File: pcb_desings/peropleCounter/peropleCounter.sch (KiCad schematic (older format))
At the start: 7 parts

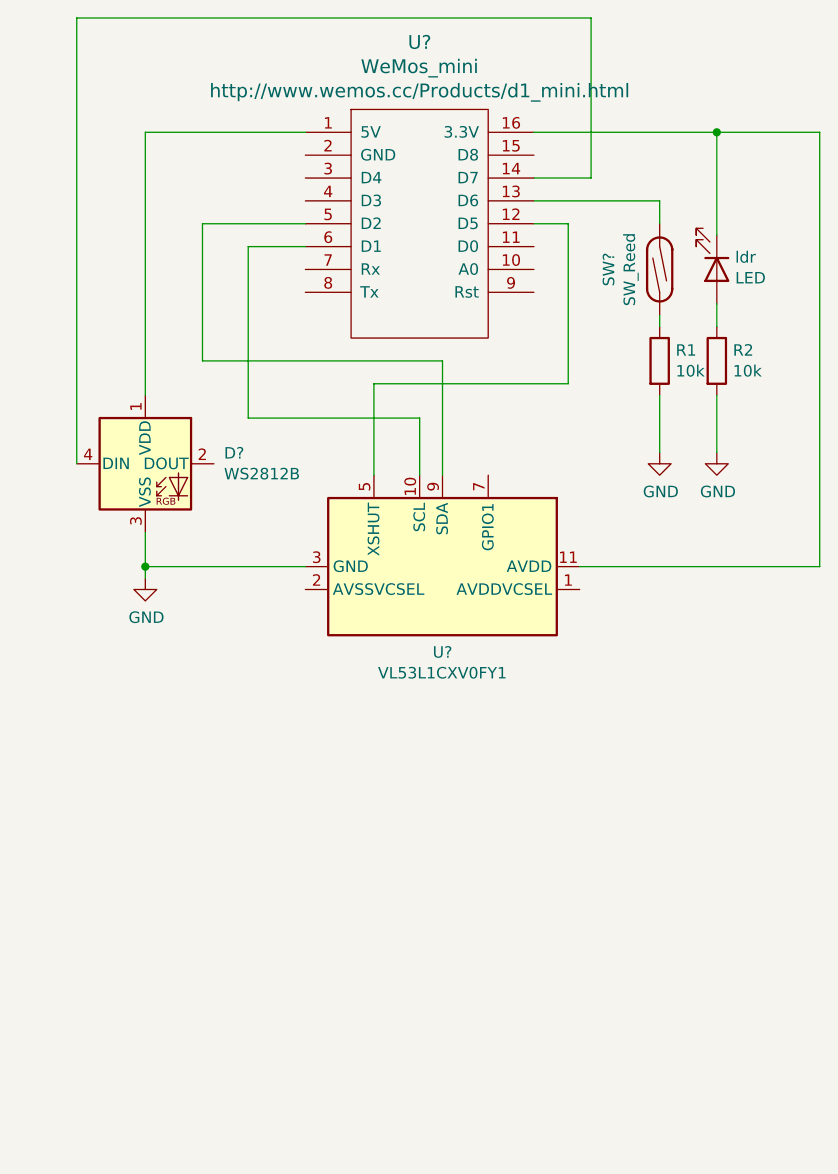
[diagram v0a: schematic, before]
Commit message: Fixed reed switch connection diagram and pin input
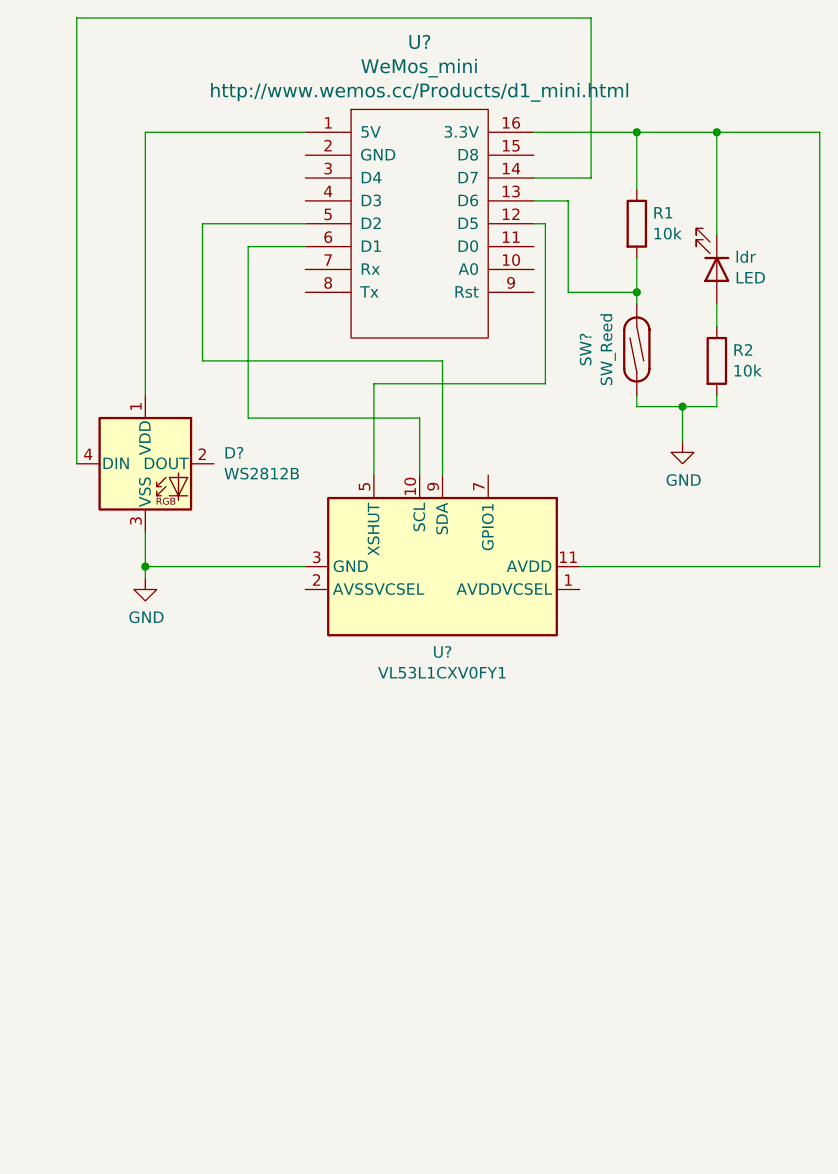
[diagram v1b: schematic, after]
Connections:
- net GND: now also SW?.1; no longer R1.2
- net at SW?.2, U?.13 (D6): now also R1.2
- net at U?.11 (AVDD), U?.16 (3.3V), ldr.1 (K): now also R1.1
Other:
- moved on the sheet: R1, SW?
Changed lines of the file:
@@
-$EndComp
-$Comp
-L Device:R R1
-U 1 1 60685B83
-P 3500 2250
-F 0 "R1" H 3570 2296 50  0000 L CNN
-F 1 "10k" H 3570 2205 50  0000 L CNN
-F 2 "" V 3430 2250 50  0001 C CNN
-F 3 "~" H 3500 2250 50  0001 C CNN
-	1    3500 2250
-	1    0    0    -1
-$EndComp
-$Comp
-L Switch:SW_Reed SW?
-U 1 1 60687B72
-P 3500 1850
-F 0 "SW?" H 3500 2072 50  0000 C CNN
-F 1 "SW_Reed" H 3500 1981 50  0000 C CNN
-F 2 "" H 3500 1850 50  0001 C CNN
-F 3 "~" H 3500 1850 50  0001 C CNN
-	1    3500 1850
-	0    -1   -1   0
 $EndComp
 $Comp
@@
 Wire Wire Line
 	3750 2100 3750 2000
-$Comp
-L power:GND #PWR?
-U 1 1 6068DD9C
-P 3750 2650
-F 0 "#PWR?" H 3750 2400 50  0001 C CNN
-F 1 "GND" H 3755 2477 50  0000 C CNN
-F 2 "" H 3750 2650 50  0001 C CNN
-F 3 "" H 3750 2650 50  0001 C CNN
-	1    3750 2650
-	1    0    0    -1
-$EndComp
-Wire Wire Line
-	3750 2650 3750 2400
-Wire Wire Line
-	2950 1250 3750 1250
-Wire Wire Line
-	3500 2100 3500 2050
-$Comp
-L power:GND #PWR?
-U 1 1 6068FDBC
-P 3500 2650
-F 0 "#PWR?" H 3500 2400 50  0001 C CNN
-F 1 "GND" H 3505 2477 50  0000 C CNN
-F 2 "" H 3500 2650 50  0001 C CNN
-F 3 "" H 3500 2650 50  0001 C CNN
-	1    3500 2650
-	1    0    0    -1
-$EndComp
-Wire Wire Line
-	3500 2650 3500 2400
 Wire Wire Line
 	1250 2400 1250 1250
@@
 	2250 2750 2250 2350
 Wire Wire Line
-	2250 2350 3100 2350
-Wire Wire Line
-	3100 2350 3100 1650
-Wire Wire Line
-	3100 1650 2950 1650
-Wire Wire Line
-	2950 1550 3500 1550
-Wire Wire Line
-	3500 1550 3500 1650
+	2250 2350 3000 2350
 Wire Wire Line
 	1950 3150 1250 3150
@@
 Wire Wire Line
 	950  750  950  2700
+$Comp
+L Switch:SW_Reed SW?
+U 1 1 60687B72
+P 3400 2200
+F 0 "SW?" H 3400 2422 50  0000 C CNN
+F 1 "SW_Reed" H 3400 2331 50  0000 C CNN
+F 2 "" H 3400 2200 50  0001 C CNN
+F 3 "~" H 3400 2200 50  0001 C CNN
+	1    3400 2200
+	0    -1   -1   0
+$EndComp
+$Comp
+L Device:R R1
+U 1 1 60685B83
+P 3400 1650
+F 0 "R1" H 3470 1696 50  0000 L CNN
+F 1 "10k" H 3470 1605 50  0000 L CNN
+F 2 "" V 3330 1650 50  0001 C CNN
+F 3 "~" H 3400 1650 50  0001 C CNN
+	1    3400 1650
+	1    0    0    -1
+$EndComp
+Wire Wire Line
+	2950 1250 3400 1250
+Wire Wire Line
+	3000 1650 3000 2350
+Wire Wire Line
+	3000 1650 2950 1650
+Wire Wire Line
+	3400 1950 3100 1950
+Wire Wire Line
+	3100 1950 3100 1550
+Wire Wire Line
+	3100 1550 2950 1550
+Connection ~ 3400 1950
+Wire Wire Line
+	3400 1950 3400 2000
+Wire Wire Line
+	3400 1500 3400 1250
+Connection ~ 3400 1250
+Wire Wire Line
+	3400 1250 3750 1250
+$Comp
+L power:GND #PWR?
+U 1 1 607608E6
+P 3600 2600
+F 0 "#PWR?" H 3600 2350 50  0001 C CNN
+F 1 "GND" H 3605 2427 50  0000 C CNN
+F 2 "" H 3600 2600 50  0001 C CNN
+F 3 "" H 3600 2600 50  0001 C CNN
+	1    3600 2600
+	1    0    0    -1
+$EndComp
+Wire Wire Line
+	3750 2400 3750 2450
+Wire Wire Line
+	3750 2450 3600 2450
+Wire Wire Line
+	3600 2450 3600 2600
+Wire Wire Line
+	3400 2450 3600 2450
+Connection ~ 3600 2450
+Wire Wire Line
+	3400 1800 3400 1950
+Wire Wire Line
+	3400 2450 3400 2400
 $EndSCHEMATC

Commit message: Updated pcb schema
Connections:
- net GND: now also U?.2 (AVSSVCSEL)
- net at U?.10 (A0): now also R2.1, ldr.1 (K)
- net at R1.1, U?.11 (AVDD), U?.16 (3.3V): now also ldr.2 (A); no longer ldr.1 (K)
- net +3V3: now reaches U?.1 (AVDDVCSEL)
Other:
- moved on the sheet: ldr
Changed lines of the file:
@@
 U 1 1 6068A202
 P 3750 1850
-F 0 "ldr" V 3697 1930 50  0000 L CNN
-F 1 "LED" V 3788 1930 50  0000 L CNN
+F 0 "ldr" V 3750 1650 50  0000 L CNN
+F 1 "LED" V 3850 1650 50  0000 L CNN
 F 2 "" H 3750 1850 50  0001 C CNN
 F 3 "~" H 3750 1850 50  0001 C CNN
 	1    3750 1850
-	0    1    1    0
+	0    -1   -1   0
 $EndComp
 Wire Wire Line
@@
 	2250 2350 3000 2350
 Wire Wire Line
-	1950 3150 1250 3150
+	1950 3150 1700 3150
 Connection ~ 1250 3150
 Wire Wire Line
@@
 Wire Wire Line
 	3400 2450 3400 2400
+Wire Wire Line
+	3750 2000 3550 2000
+Wire Wire Line
+	3550 2000 3550 1850
+Wire Wire Line
+	3550 1850 2950 1850
+Connection ~ 3750 2000
+Wire Wire Line
+	1950 3250 1700 3250
+Wire Wire Line
+	1700 3250 1700 3150
+Connection ~ 1700 3150
+Wire Wire Line
+	1700 3150 1250 3150
+$Comp
+L power:+3V3 #PWR?
+U 1 1 60992C22
+P 3300 3250
+F 0 "#PWR?" H 3300 3100 50  0001 C CNN
+F 1 "+3V3" V 3300 3400 50  0000 L CNN
+F 2 "" H 3300 3250 50  0001 C CNN
+F 3 "" H 3300 3250 50  0001 C CNN
+	1    3300 3250
+	0    1    1    0
+$EndComp
+Wire Wire Line
+	3150 3250 3300 3250
 $EndSCHEMATC

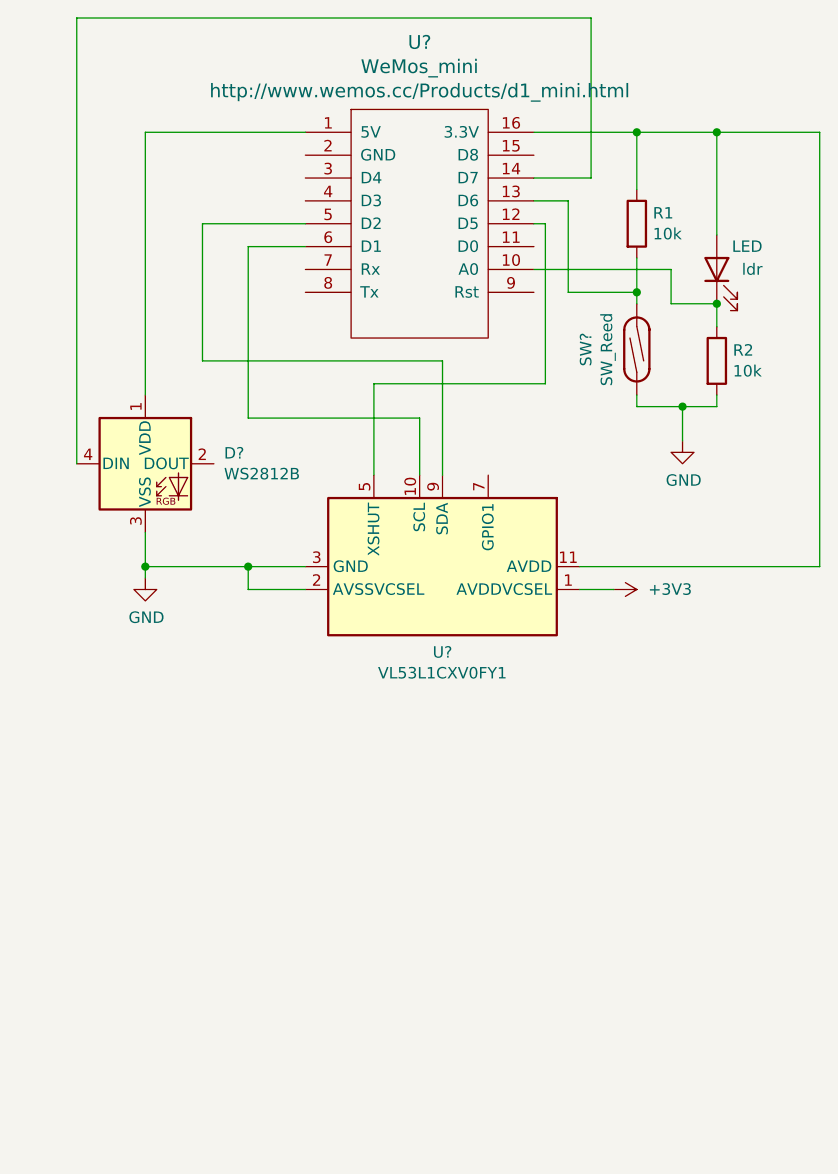
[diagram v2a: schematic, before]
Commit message: Connect ToF GPIO to wemos D8
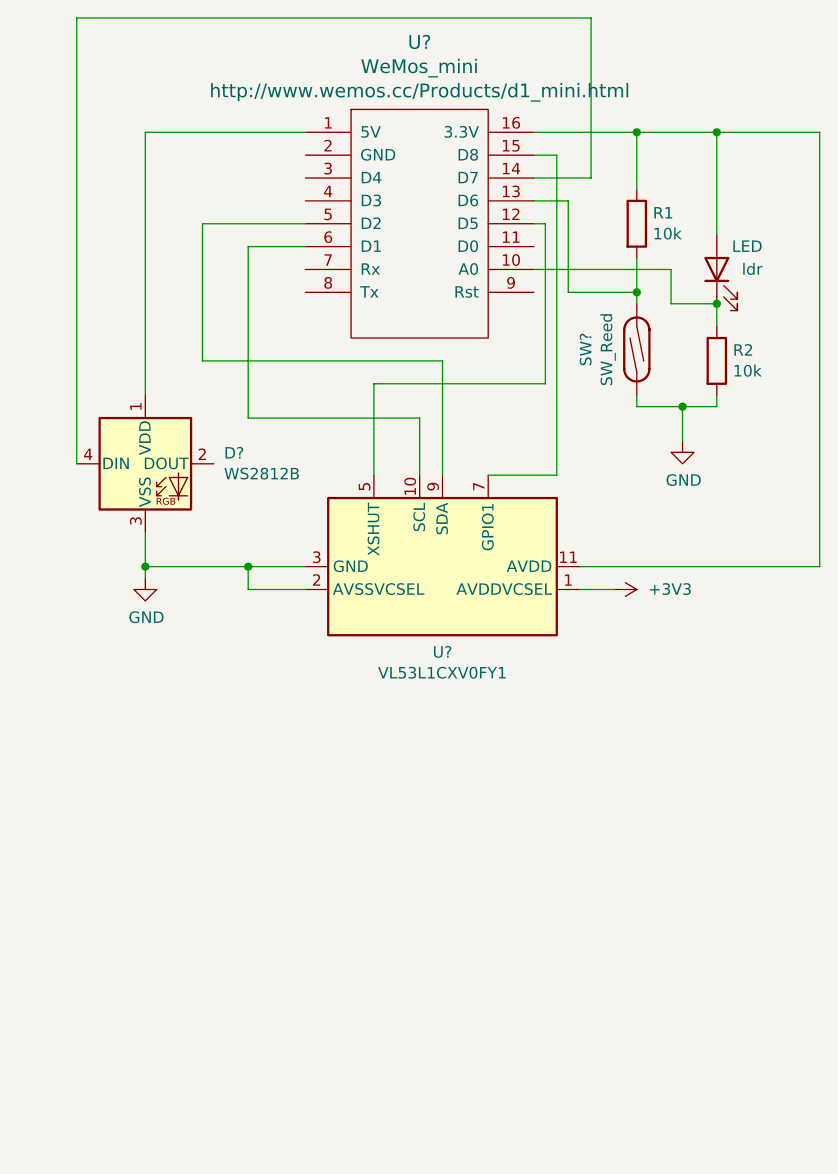
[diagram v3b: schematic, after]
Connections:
- net at U?.15 (D8): now also U?.7 (GPIO1)
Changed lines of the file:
@@
 Wire Wire Line
 	3150 3250 3300 3250
+Wire Wire Line
+	2750 2750 3050 2750
+Wire Wire Line
+	3050 2750 3050 1350
+Wire Wire Line
+	3050 1350 2950 1350
 $EndSCHEMATC

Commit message: Updated peopleCounter board sch
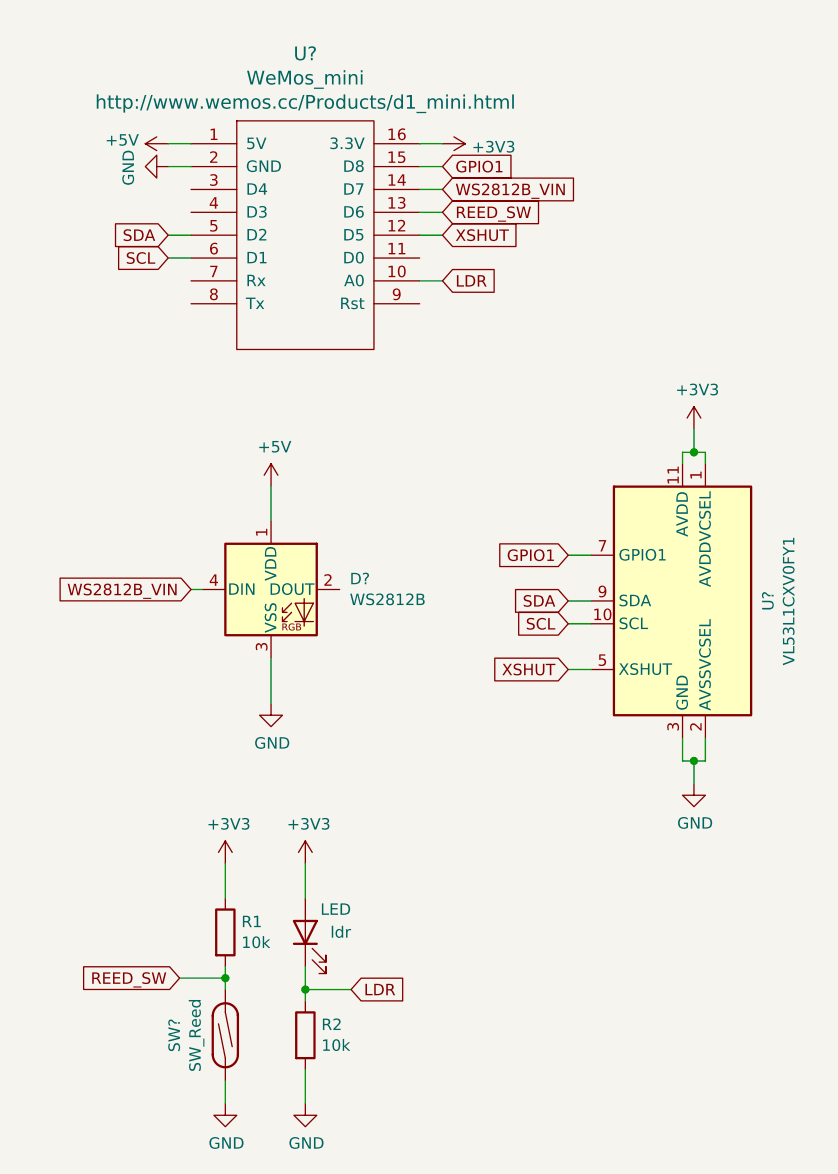
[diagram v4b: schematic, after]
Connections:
- net +3V3: now also R1.1, U?.11 (AVDD), U?.16 (3.3V), ldr.2 (A)
- net GND: now also U?.2 (GND)
- net +5V: now reaches D?.1 (VDD), U?.1 (5V)
- net LDR: now reaches R2.1, U?.10 (A0), ldr.1 (K)
- net XSHUT: now reaches U?.12 (D5), U?.5 (XSHUT)
- net REED_SW: now reaches R1.2, SW?.2, U?.13 (D6)
- net WS2812B_VIN: now reaches D?.4 (DIN), U?.14 (D7)
- net GPIO1: now reaches U?.15 (D8), U?.7 (GPIO1)
- net SDA: now reaches U?.5 (D2), U?.9 (SDA)
- net SCL: now reaches U?.10 (SCL), U?.6 (D1)
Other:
- moved on the sheet: D?, R1, R2, SW?, U?, ldr
